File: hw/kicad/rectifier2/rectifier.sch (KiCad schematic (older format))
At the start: 64 parts, among them J1 CONN_01X04, J2 DIL16, P1 CONN_01X03, P2 CONN_01X02, P3 CONN_01X02, P4 CONN_01X02, Q2 Q_NMOS_GDS, Q3 Q_NMOS_GDS, U1 ACT4088, U2 STM32F042F6Px, U3 lnk304D

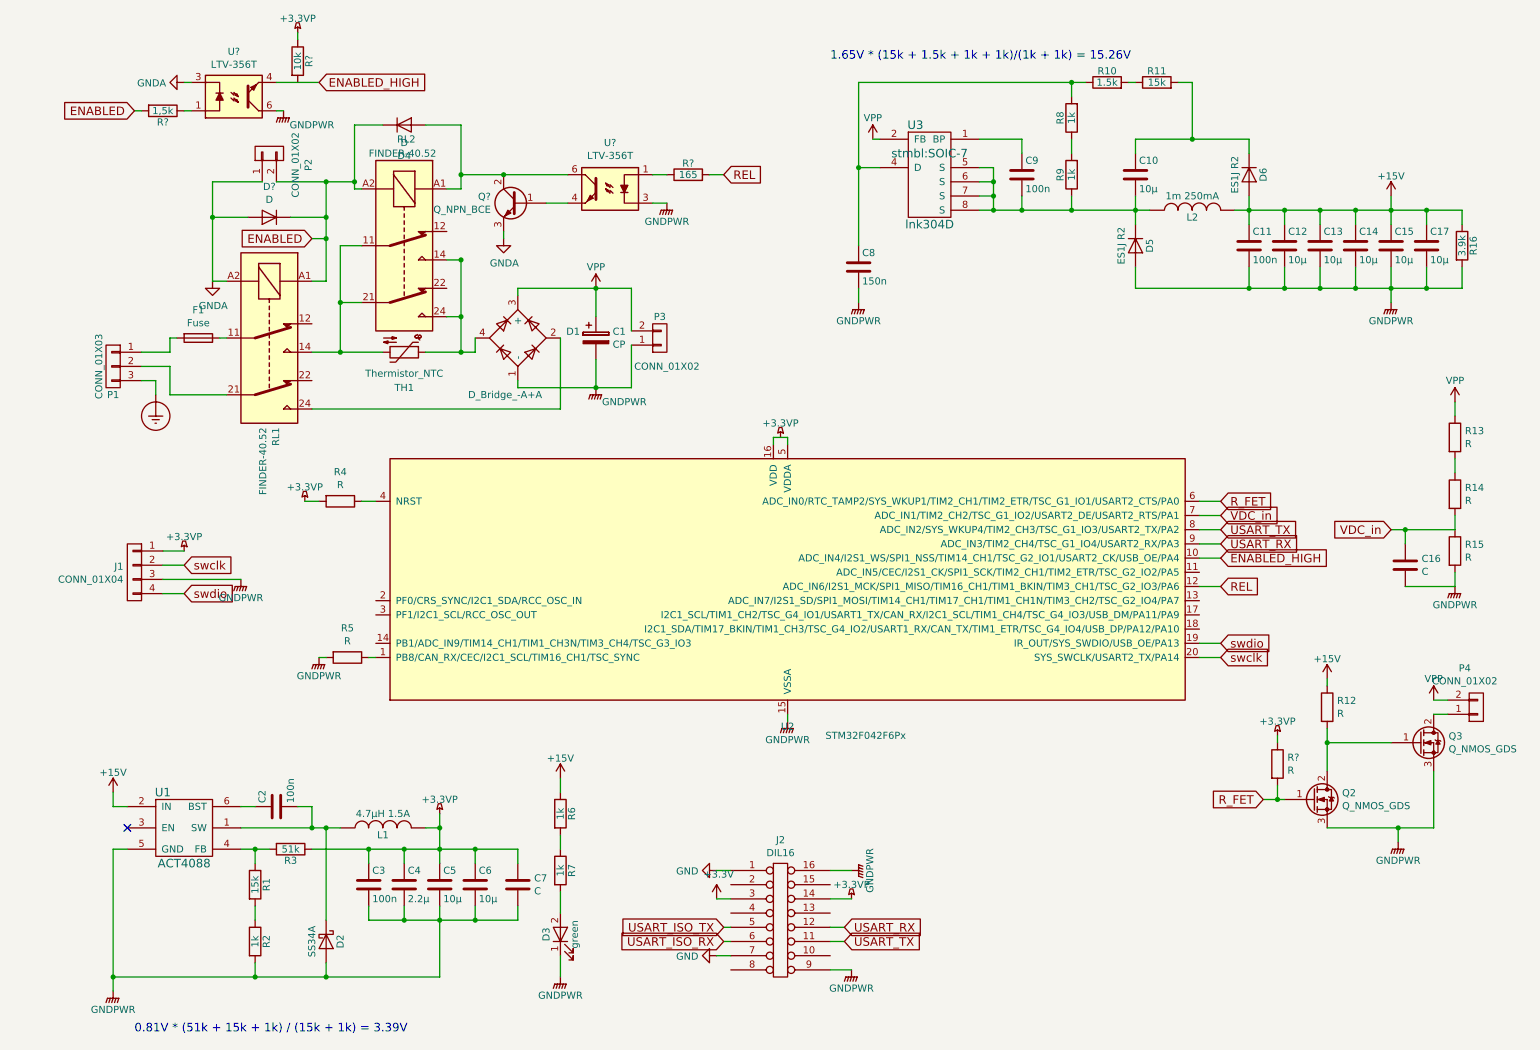
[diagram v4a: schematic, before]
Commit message: First full route of the rectifier board with braking resistor. Clearances should be large enough for mains applications. Some strange junctions remain.
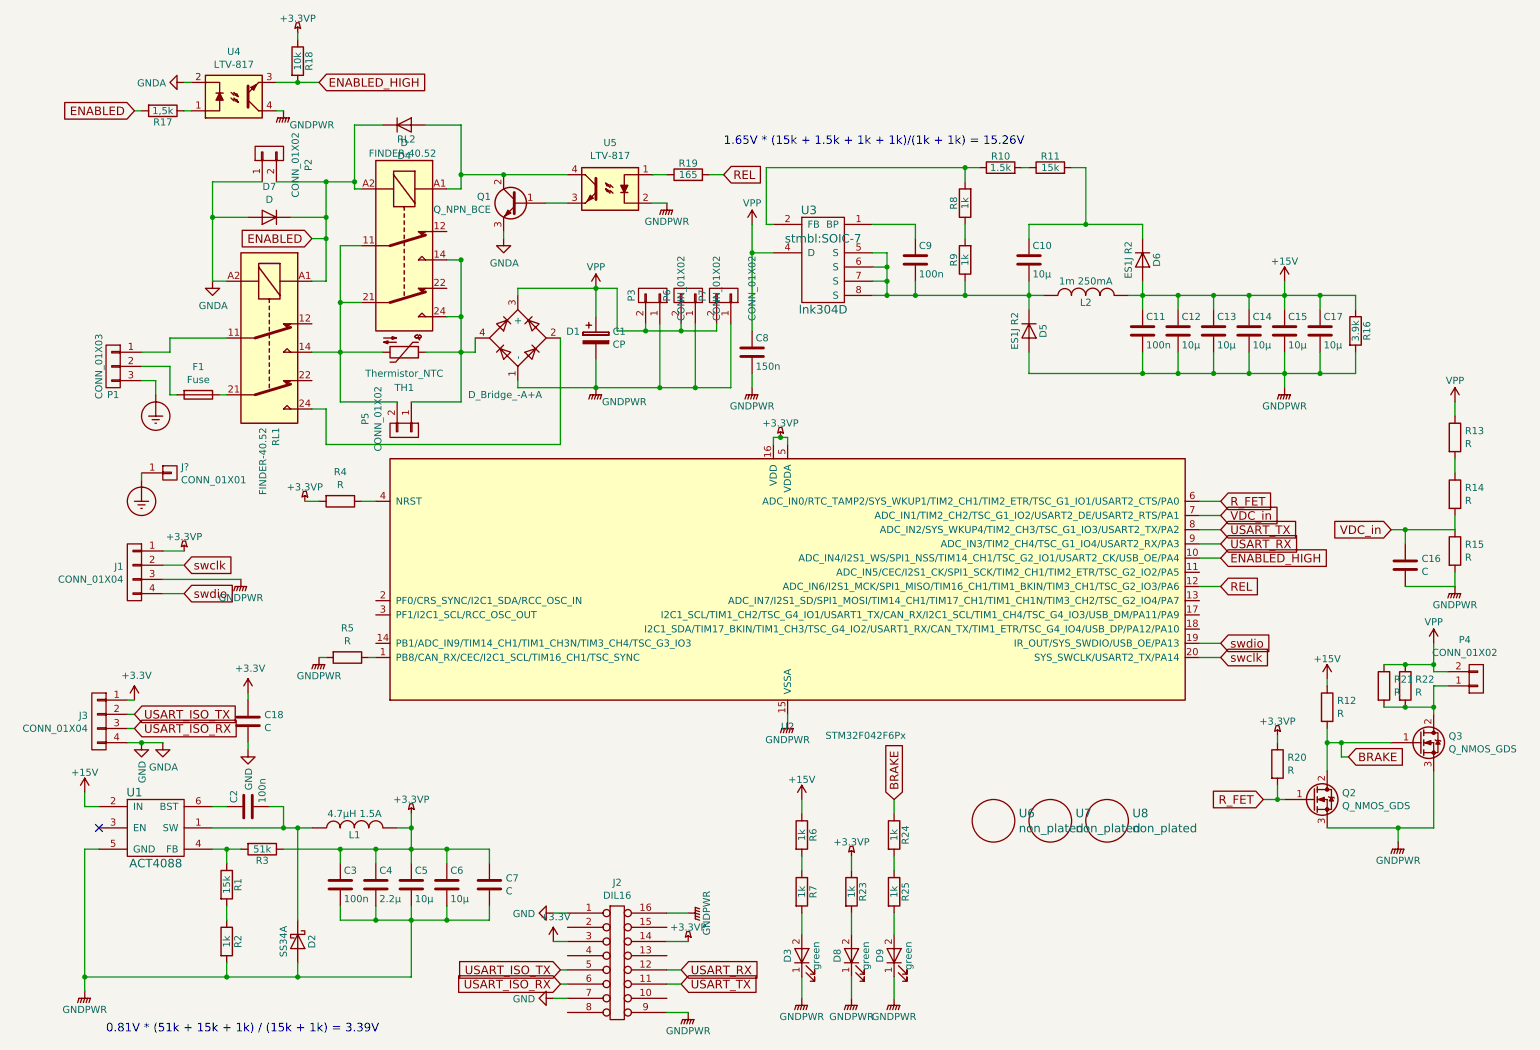
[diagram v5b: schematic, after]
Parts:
- removed U? (x2): LTV-356T, Housings_DIP:DIP-6_W7.62mm_SMD, symbol LTV-356T
- added C18: C, stmbl:C_0603, symbol C
- added D8, D9: green, stmbl:LED-0805-SIDE, symbol LED
- added J3: CONN_01X04, Pin_Headers:Pin_Header_Straight_1x04, symbol CONN_01X04
- added J?: CONN_01X01, symbol CONN_01X01
- added P5, P6, P7: CONN_01X02, stmbl:RM5.08_1x2, symbol CONN_01X02
- added R21, R22: R, Diodes_ThroughHole:Diode_TO-247_Horizontal_largePads, symbol R
- added R23, R24, R25: 1k, stmbl:R_0603, symbol R
- added U4, U5: LTV-817, Opto-Devices:Optocoupler_SMD_HandSoldering_KPC357_LTV35x_PC357_SingleChannel, symbol LTV-817
- added U6, U7, U8: non_plated, Mounting_Holes:MountingHole_3.2mm_M3, symbol non_plated
- C1: footprint Capacitors_ThroughHole:CP_Radial_D35.0mm_P10.00mm_SnapIn -> Capacitors_ThroughHole:C_Radial_D26_L31_P10
- C16, C7: footprint (none) -> stmbl:C_0603
- D4: footprint (none) -> stmbl:SMA_Standard
- D7: renamed from D?; footprint (none) -> stmbl:SMA_Standard
- J1: footprint (none) -> Pin_Headers:Pin_Header_Straight_1x04
- J2: footprint (none) -> SMD_Packages:SO-16-W
- Q1: renamed from Q?; footprint (none) -> stmbl:SOT-23
- Q2: footprint (none) -> stmbl:SOT-23
- Q3: footprint (none) -> TO_SOT_Packages_THT:TO-247_Horizontal_Neutral123_largePads
- R12, R15, R4, R5: footprint (none) -> stmbl:R_0603
- R13, R14: footprint (none) -> stmbl:R_1206
- R20: renamed from R?; footprint (none) -> stmbl:R_0603
- gave numbers to parts that had none: 3
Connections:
- net GNDA is gone; now on net GND: D7.2 (A), P2.1 (P1), Q1.3 (E), RL1.A2
- net +3.3VP: now also U2.16 (VDD), U2.5 (VDDA), R23.1
- net +3V3: now also C18.1, J3.1 (P1)
- net ENABLED_HIGH: now also R18.2, U4.3
- net Earth_Protective: now also J?.1 (P1)
- net GND: now also C18.2, J3.4 (P4), U4.2
- net GNDPWR: now also D8.1 (K), D9.1 (K), P6.1 (P1), P7.1 (P1), U4.4, U5.2
- net USART_ISO_RX: now also J3.3 (P3)
- net USART_ISO_TX: now also J3.2 (P2)
- net VPP: now also C8.1, U3.4 (D), P6.2 (P2), P7.2 (P2), R21.1, R22.1; no longer U3.2 (FB)
- net at P1.1 (P1): now also RL1.11; no longer F1.2
- net at P1.2 (P2): now also F1.2; no longer RL1.21
- net at F1.1: now also RL1.21; no longer RL1.11
- net at RL1.14, RL2.11, RL2.21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: now also P5.2 (P2)
- net at D1.4, RL2.14, RL2.24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: now also P5.1 (P1)
- net at D4.2 (A), Q1.2 (C), RL2.A1: now also U5.4
- net at R10.1, R8.2: now also U3.2 (FB); no longer C8.1, U3.4 (D)
- net BRAKE: now reaches Q2.2 (D), Q3.1 (G), R12.2
- net BRAKE: now also R24.1
- net at P4.1 (P1), Q3.2 (D): now also R21.2, R22.2
- net at R19.1: now also U5.1
- net at Q1.1 (B): now also U5.3
- net at R17.1: now also U4.1
- new net: D8.2 (A), R23.2
- new net: D9.2 (A), R25.2
- new net: R24.2, R25.1
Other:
- moved on the sheet: C10, C11, C12, C13, C14, C15, C17, C2, C3, C4, C5, C6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

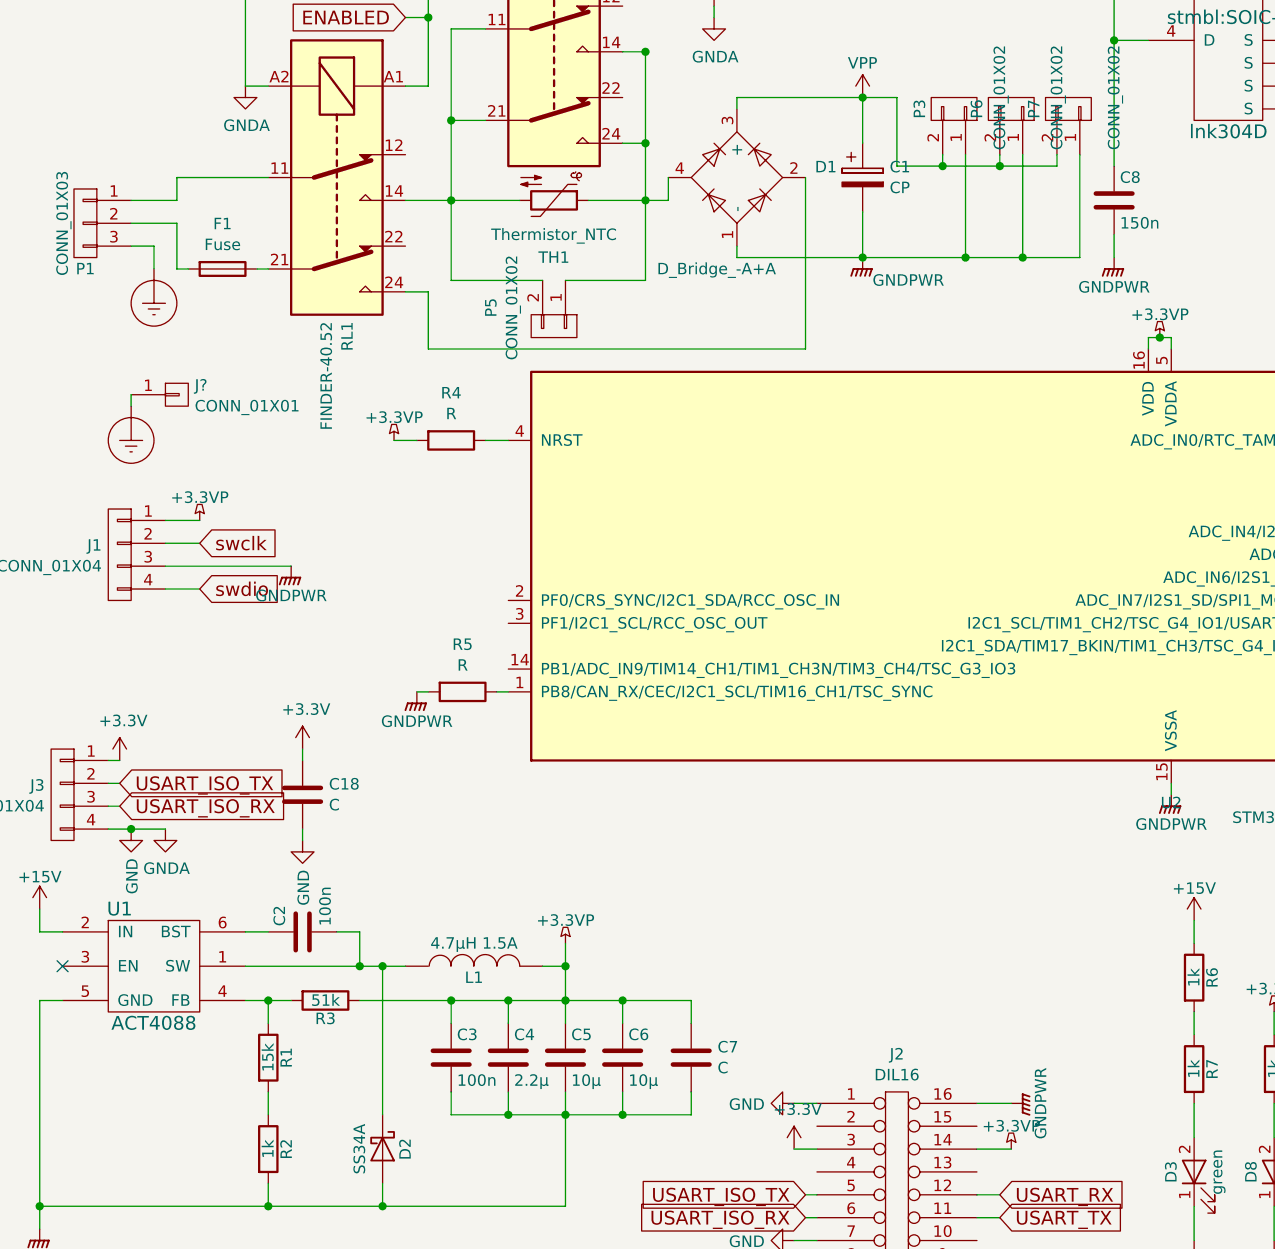
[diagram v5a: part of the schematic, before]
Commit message: Small changes. Fixed SWD pinout + zones + caps on VPP
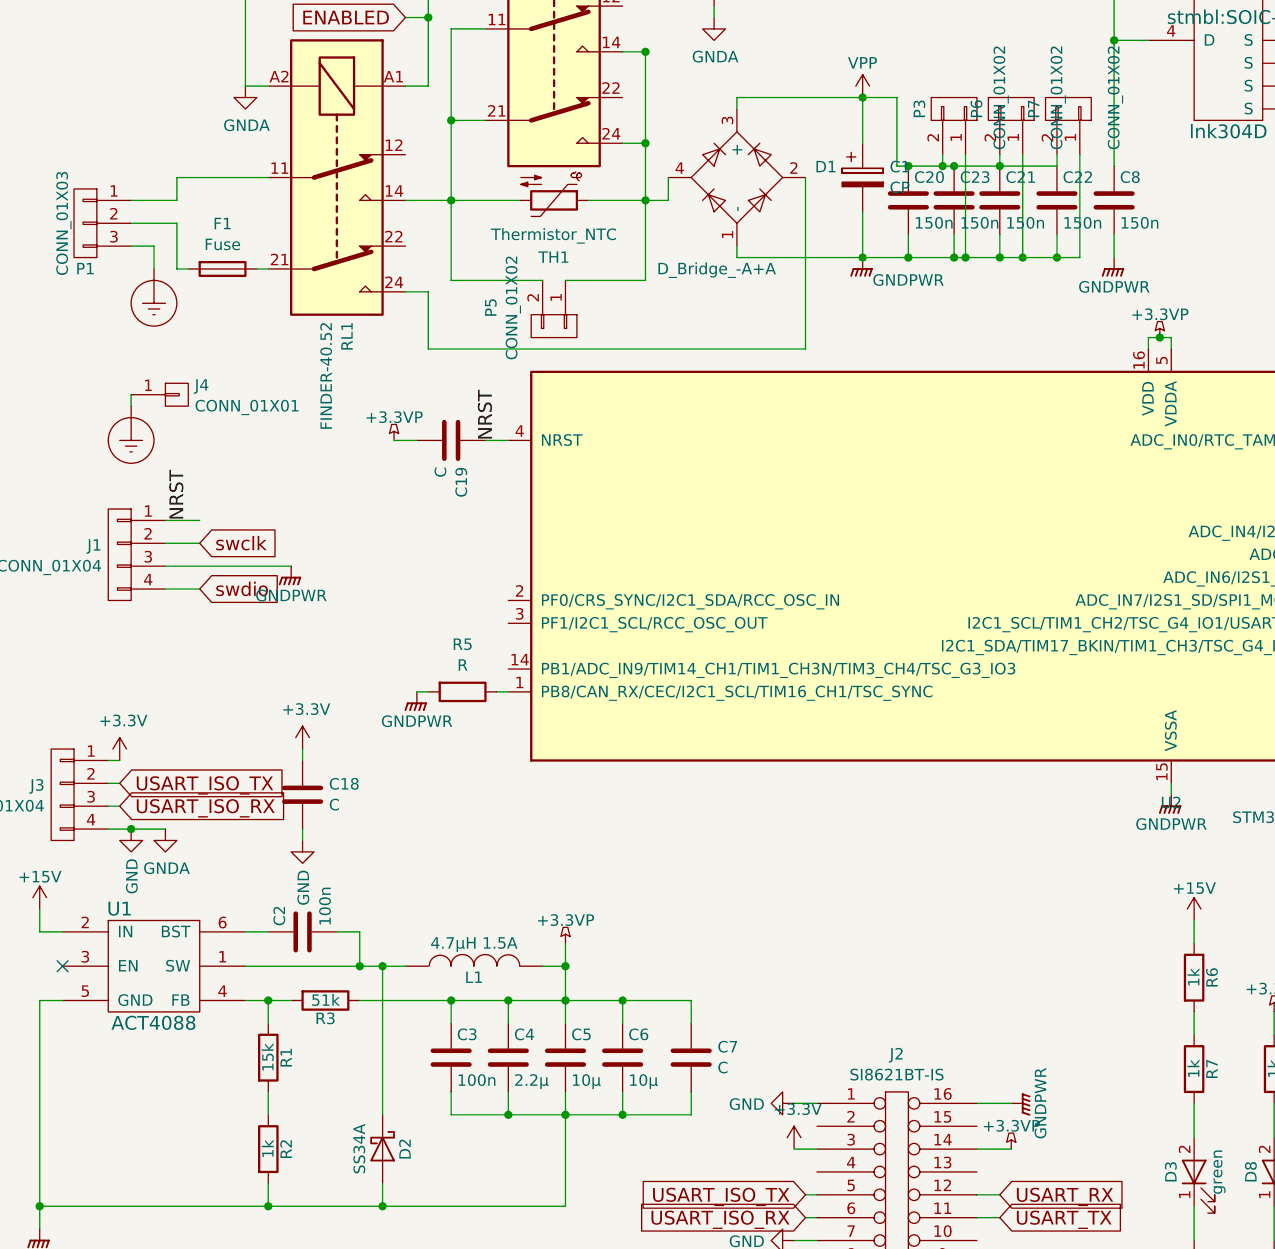
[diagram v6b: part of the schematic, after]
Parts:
- removed R4: R, stmbl:R_0603, symbol R
- added C19: C, stmbl:C_0603, symbol C
- added C20, C21, C22, C23: 150n, stmbl:C_1808, symbol C
- J2: value DIL16 -> SI8621BT-IS
- J4: renamed from J?; footprint (none) -> Mounting_Holes:MountingHole_3.2mm_M3
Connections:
- net +3.3VP: now also C19.2; no longer J1.1 (P1)
- net GNDPWR: now also C20.2, C21.2, C22.2, C23.2
- net VPP: now also C20.1, C21.1, C22.1, C23.1
- net NRST: now reaches U2.4 (NRST)
- net NRST: now also J1.1 (P1), C19.1

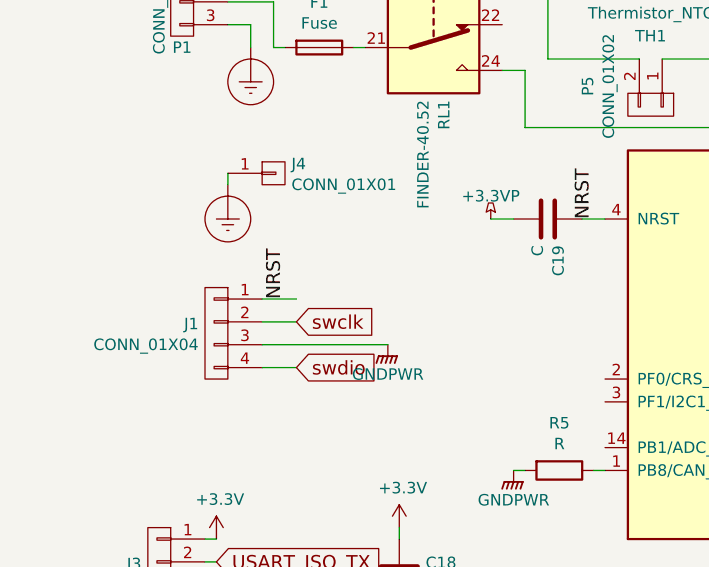
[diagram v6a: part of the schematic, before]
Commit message: Fix SWD again. Some small changes.
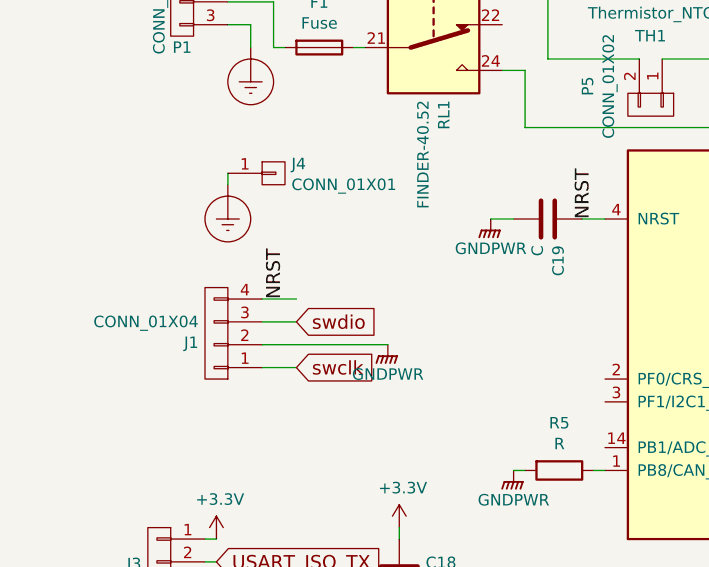
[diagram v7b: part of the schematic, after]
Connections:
- net +3.3VP: no longer C19.2
- net GNDPWR: now also C19.2, J1.2 (P2); no longer J1.3 (P3)
- net NRST: now also J1.4 (P4); no longer J1.1 (P1)
- net swclk: now also J1.1 (P1); no longer J1.2 (P2)
- net swdio: now also J1.3 (P3); no longer J1.4 (P4)
